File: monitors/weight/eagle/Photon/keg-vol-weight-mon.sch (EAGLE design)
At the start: 18 parts

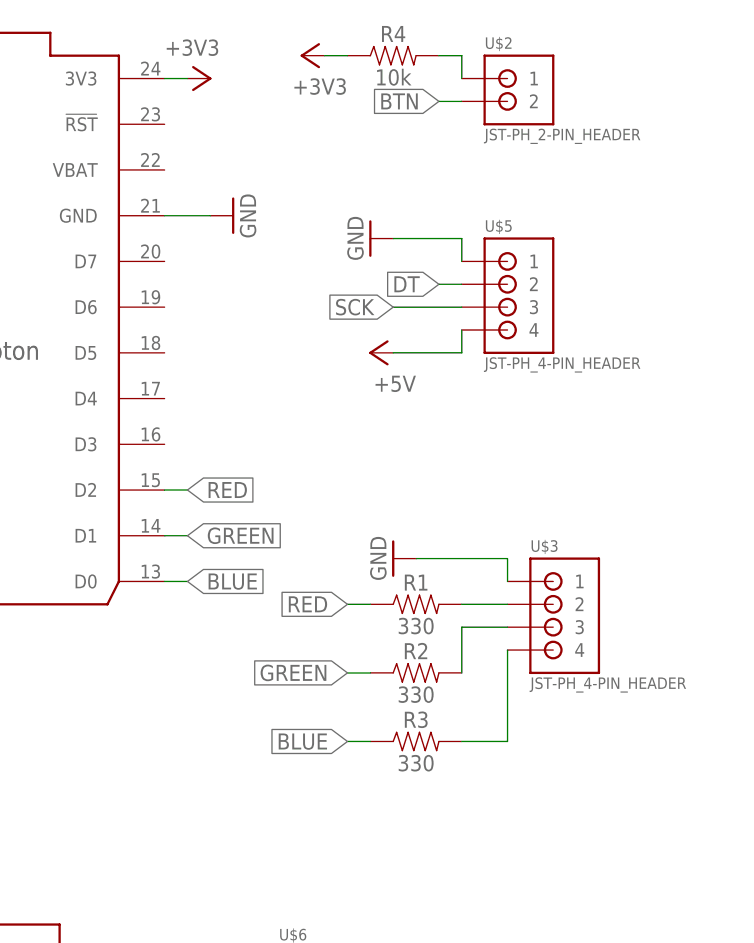
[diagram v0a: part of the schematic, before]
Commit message: Got the device registration process working
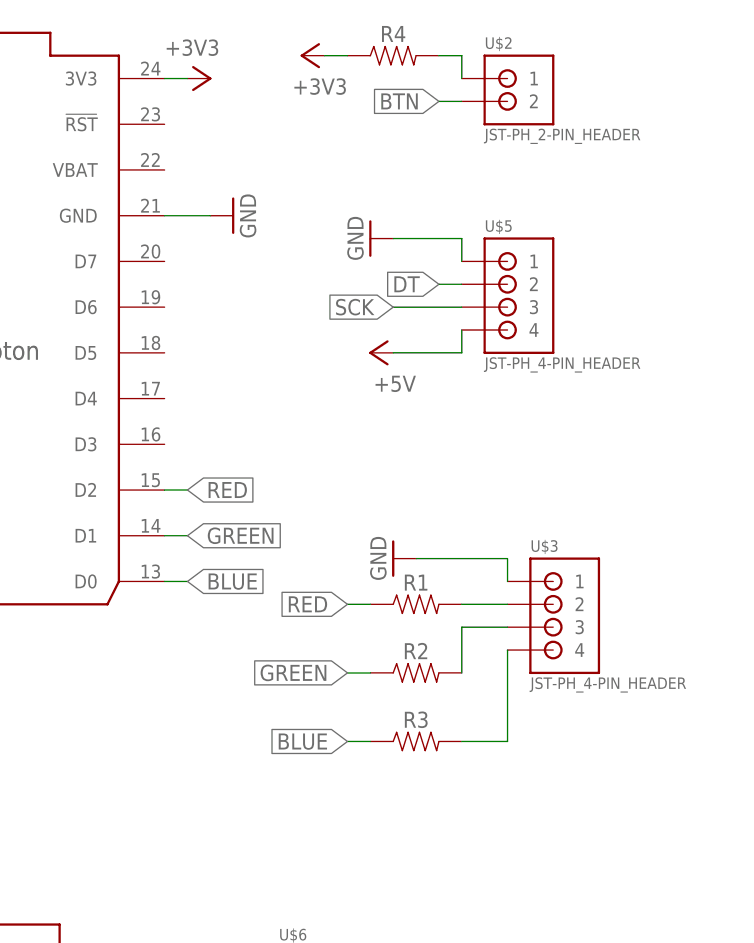
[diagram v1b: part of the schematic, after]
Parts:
- R1, R2, R3: value 330 -> (none)
- R4: value 10k -> (none)
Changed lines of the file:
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@@
 <grid distance="0.1" unitdist="inch" unit="inch" style="lines" multiple="1" display="no" altdistance="0.01" altunitdist="inch" altunit="inch"/>
 <layers>
-<layer number="1" name="Top" color="4" fill="1" visible="yes" active="no"/>
-<layer number="16" name="Bottom" color="1" fill="1" visible="yes" active="no"/>
-<layer number="17" name="Pads" color="2" fill="1" visible="yes" active="no"/>
-<layer number="18" name="Vias" color="2" fill="1" visible="yes" active="no"/>
-<layer number="19" name="Unrouted" color="6" fill="1" visible="yes" active="no"/>
-<layer number="20" name="Dimension" color="15" fill="1" visible="yes" active="no"/>
-<layer number="21" name="tPlace" color="7" fill="1" visible="yes" active="no"/>
-<layer number="22" name="bPlace" color="7" fill="1" visible="yes" active="no"/>
-<layer number="23" name="tOrigins" color="15" fill="1" visible="yes" active="no"/>
-<layer number="24" name="bOrigins" color="15" fill="1" visible="yes" active="no"/>
-<layer number="25" name="tNames" color="7" fill="1" visible="yes" active="no"/>
-<layer number="26" name="bNames" color="7" fill="1" visible="yes" active="no"/>
-<layer number="27" name="tValues" color="7" fill="1" visible="yes" active="no"/>
-<layer number="28" name="bValues" color="7" fill="1" visible="yes" active="no"/>
+<layer number="1" name="Top" color="4" fill="1" visible="no" active="no"/>
+<layer number="16" name="Bottom" color="1" fill="1" visible="no" active="no"/>
+<layer number="17" name="Pads" color="2" fill="1" visible="no" active="no"/>
+<layer number="18" name="Vias" color="2" fill="1" visible="no" active="no"/>
+<layer number="19" name="Unrouted" color="6" fill="1" visible="no" active="no"/>
+<layer number="20" name="Dimension" color="15" fill="1" visible="no" active="no"/>
+<layer number="21" name="tPlace" color="7" fill="1" visible="no" active="no"/>
+<layer number="22" name="bPlace" color="7" fill="1" visible="no" active="no"/>
+<layer number="23" name="tOrigins" color="15" fill="1" visible="no" active="no"/>
+<layer number="24" name="bOrigins" color="15" fill="1" visible="no" active="no"/>
+<layer number="25" name="tNames" color="7" fill="1" visible="no" active="no"/>
+<layer number="26" name="bNames" color="7" fill="1" visible="no" active="no"/>
+<layer number="27" name="tValues" color="7" fill="1" visible="no" active="no"/>
+<layer number="28" name="bValues" color="7" fill="1" visible="no" active="no"/>
 <layer number="29" name="tStop" color="7" fill="3" visible="no" active="no"/>
 <layer number="30" name="bStop" color="7" fill="6" visible="no" active="no"/>
@@
 <layer number="35" name="tGlue" color="7" fill="4" visible="no" active="no"/>
 <layer number="36" name="bGlue" color="7" fill="5" visible="no" active="no"/>
-<layer number="37" name="tTest" color="7" fill="1" visible="yes" active="no"/>
-<layer number="38" name="bTest" color="7" fill="1" visible="yes" active="no"/>
+<layer number="37" name="tTest" color="7" fill="1" visible="no" active="no"/>
+<layer number="38" name="bTest" color="7" fill="1" visible="no" active="no"/>
 <layer number="39" name="tKeepout" color="4" fill="11" visible="no" active="no"/>
 <layer number="40" name="bKeepout" color="1" fill="11" visible="no" active="no"/>
@@
 <layer number="44" name="Drills" color="7" fill="1" visible="no" active="no"/>
 <layer number="45" name="Holes" color="7" fill="1" visible="no" active="no"/>
-<layer number="46" name="Milling" color="3" fill="1" visible="yes" active="no"/>
-<layer number="47" name="Measures" color="7" fill="1" visible="yes" active="no"/>
-<layer number="48" name="Document" color="7" fill="1" visible="yes" active="no"/>
-<layer number="49" name="Reference" color="7" fill="1" visible="yes" active="no"/>
-<layer number="50" name="dxf" color="7" fill="1" visible="yes" active="no"/>
-<layer number="51" name="tDocu" color="14" fill="1" visible="yes" active="no"/>
-<layer number="52" name="bDocu" color="7" fill="1" visible="yes" active="no"/>
-<layer number="53" name="tGND_GNDA" color="7" fill="9" visible="yes" active="no"/>
-<layer number="54" name="bGND_GNDA" color="1" fill="9" visible="yes" active="no"/>
-<layer number="56" name="wert" color="7" fill="1" visible="yes" active="no"/>
-<layer number="57" name="tCAD" color="7" fill="1" visible="yes" active="no"/>
-<layer number="58" name="bCopper" color="7" fill="1" visible="yes" active="no"/>
-<layer number="59" name="tCarbon" color="7" fill="1" visible="yes" active="no"/>
-<layer number="60" name="bCarbon" color="7" fill="1" visible="yes" active="no"/>
+<layer number="46" name="Milling" color="3" fill="1" visible="no" active="no"/>
+<layer number="47" name="Measures" color="7" fill="1" visible="no" active="no"/>
+<layer number="48" name="Document" color="7" fill="1" visible="no" active="no"/>
+<layer number="49" name="Reference" color="7" fill="1" visible="no" active="no"/>
+<layer number="50" name="dxf" color="7" fill="1" visible="no" active="no"/>
+<layer number="51" name="tDocu" color="14" fill="1" visible="no" active="no"/>
+<layer number="52" name="bDocu" color="7" fill="1" visible="no" active="no"/>
+<layer number="53" name="tGND_GNDA" color="7" fill="9" visible="no" active="no"/>
+<layer number="54" name="bGND_GNDA" color="1" fill="9" visible="no" active="no"/>
+<layer number="56" name="wert" color="7" fill="1" visible="no" active="no"/>
+<layer number="57" name="tCAD" color="7" fill="1" visible="no" active="no"/>
+<layer number="58" name="bCopper" color="7" fill="1" visible="no" active="no"/>
+<layer number="59" name="tCarbon" color="7" fill="1" visible="no" active="no"/>
+<layer number="60" name="bCarbon" color="7" fill="1" visible="no" active="no"/>
 <layer number="88" name="SimResults" color="9" fill="1" visible="yes" active="yes"/>
 <layer number="89" name="SimProbes" color="9" fill="1" visible="yes" active="yes"/>
@@
 <parts>
 <part name="U$1" library="Particle-Devices" deviceset="PHOTON" device="_WITH_HEADERS" package3d_urn="urn:adsk.eagle:package:5952920/2"/>
-<part name="R1" library="SparkFun-Resistors" library_urn="urn:adsk.eagle:library:532" deviceset="RESISTOR" device="AXIAL-0.3" package3d_urn="urn:adsk.eagle:package:39658/2" value="330"/>
-<part name="R2" library="SparkFun-Resistors" library_urn="urn:adsk.eagle:library:532" deviceset="RESISTOR" device="AXIAL-0.3" package3d_urn="urn:adsk.eagle:package:39658/2" value="330"/>
-<part name="R3" library="SparkFun-Resistors" library_urn="urn:adsk.eagle:library:532" deviceset="RESISTOR" device="AXIAL-0.3" package3d_urn="urn:adsk.eagle:package:39658/2" value="330"/>
+<part name="R1" library="SparkFun-Resistors" library_urn="urn:adsk.eagle:library:532" deviceset="RESISTOR" device="AXIAL-0.3" package3d_urn="urn:adsk.eagle:package:39658/2" value=" "/>
+<part name="R2" library="SparkFun-Resistors" library_urn="urn:adsk.eagle:library:532" deviceset="RESISTOR" device="AXIAL-0.3" package3d_urn="urn:adsk.eagle:package:39658/2" value=" "/>
+<part name="R3" library="SparkFun-Resistors" library_urn="urn:adsk.eagle:library:532" deviceset="RESISTOR" device="AXIAL-0.3" package3d_urn="urn:adsk.eagle:package:39658/2" value=" "/>
 <part name="U$3" library="SRG" deviceset="JST-PH_4-PIN_HEADER" device=""/>
 <part name="U$5" library="SRG" deviceset="JST-PH_4-PIN_HEADER" device=""/>
@@
 <part name="GND6" library="supply1" library_urn="urn:adsk.eagle:library:371" deviceset="GND" device=""/>
 <part name="U$2" library="SRG" deviceset="JST-PH_2-PIN_HEADER" device=""/>
-<part name="R4" library="SparkFun-Resistors" library_urn="urn:adsk.eagle:library:532" deviceset="RESISTOR" device="AXIAL-0.3" package3d_urn="urn:adsk.eagle:package:39658/2" value="10k"/>
+<part name="R4" library="SparkFun-Resistors" library_urn="urn:adsk.eagle:library:532" deviceset="RESISTOR" device="AXIAL-0.3" package3d_urn="urn:adsk.eagle:package:39658/2" value=" "/>
 <part name="P+1" library="supply1" library_urn="urn:adsk.eagle:library:371" deviceset="+5V" device=""/>
 <part name="+3V1" library="supply1" library_urn="urn:adsk.eagle:library:371" deviceset="+3V3" device=""/>
